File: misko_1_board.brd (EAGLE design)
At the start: 115 x 115 mm, 152 parts, among them IC1 ATMEGA1281-16AU, IC10 ORG1510-MK4, IC11 TPS3808G33DBVT, IC12 LTC4425, IC13 RN4678_BT_MODULE, IC14 ADXL345, IC15 74HCT1G32, IC16 FM25W256-SOIC, IC17 MICROSD_SPI_MODE, IC18 FH12-30S-0.5SH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

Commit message: - crude device driver for the FM25W256 FeRAM SPI device
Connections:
- net SPI_FRAM_SS_PIN renamed SPI_SS_FRAM_PIN
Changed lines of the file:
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@@
 <wire x1="27.5" y1="48.93660625" x2="27.56339375" y2="49" width="0.25" layer="1"/>
 </signal>
-<signal name="SPI_FRAM_SS_PIN" class="2">
+<signal name="SPI_SS_FRAM_PIN" class="2">
 <contactref element="IC16" pad="!CS!"/>
 <contactref element="R19" pad="1"/>

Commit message: - corrected EN pulldown resistor value to 10k
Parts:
- R2: value 150k -> 10k
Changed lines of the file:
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@@
 <grid distance="0.25" unitdist="mm" unit="mm" style="lines" multiple="1" display="yes" altdistance="0.005" altunitdist="mm" altunit="mm"/>
 <layers>
-<layer number="1" name="Top" color="4" fill="1" visible="no" active="yes"/>
+<layer number="1" name="Top" color="4" fill="1" visible="yes" active="yes"/>
 <layer number="2" name="Route2" color="1" fill="3" visible="no" active="no"/>
 <layer number="3" name="Route3" color="4" fill="3" visible="no" active="no"/>
@@
 <layer number="19" name="Unrouted" color="6" fill="1" visible="yes" active="yes"/>
 <layer number="20" name="Dimension" color="15" fill="1" visible="yes" active="yes"/>
-<layer number="21" name="tPlace" color="7" fill="1" visible="no" active="yes"/>
+<layer number="21" name="tPlace" color="7" fill="1" visible="yes" active="yes"/>
 <layer number="22" name="bPlace" color="7" fill="1" visible="yes" active="yes"/>
-<layer number="23" name="tOrigins" color="15" fill="1" visible="no" active="yes"/>
+<layer number="23" name="tOrigins" color="15" fill="1" visible="yes" active="yes"/>
 <layer number="24" name="bOrigins" color="15" fill="1" visible="yes" active="yes"/>
-<layer number="25" name="tNames" color="7" fill="1" visible="no" active="yes"/>
+<layer number="25" name="tNames" color="7" fill="1" visible="yes" active="yes"/>
 <layer number="26" name="bNames" color="7" fill="1" visible="yes" active="yes"/>
 <layer number="27" name="tValues" color="7" fill="1" visible="no" active="yes"/>
@@
 <layer number="37" name="tTest" color="7" fill="1" visible="no" active="yes"/>
 <layer number="38" name="bTest" color="7" fill="1" visible="no" active="yes"/>
-<layer number="39" name="tKeepout" color="4" fill="11" visible="no" active="yes"/>
+<layer number="39" name="tKeepout" color="4" fill="11" visible="yes" active="yes"/>
 <layer number="40" name="bKeepout" color="1" fill="11" visible="yes" active="yes"/>
-<layer number="41" name="tRestrict" color="4" fill="10" visible="no" active="yes"/>
+<layer number="41" name="tRestrict" color="4" fill="10" visible="yes" active="yes"/>
 <layer number="42" name="bRestrict" color="1" fill="10" visible="yes" active="yes"/>
 <layer number="43" name="vRestrict" color="2" fill="10" visible="no" active="yes"/>
@@
 <layer number="45" name="Holes" color="7" fill="1" visible="yes" active="yes"/>
 <layer number="46" name="Milling" color="3" fill="1" visible="yes" active="yes"/>
-<layer number="47" name="Measures" color="7" fill="1" visible="yes" active="yes"/>
+<layer number="47" name="Measures" color="7" fill="1" visible="no" active="yes"/>
 <layer number="48" name="Document" color="7" fill="1" visible="yes" active="yes"/>
 <layer number="49" name="Reference" color="7" fill="1" visible="no" active="yes"/>
 <layer number="50" name="dxf" color="7" fill="1" visible="no" active="no"/>
-<layer number="51" name="tDocu" color="7" fill="1" visible="no" active="yes"/>
+<layer number="51" name="tDocu" color="7" fill="1" visible="yes" active="yes"/>
 <layer number="52" name="bDocu" color="7" fill="1" visible="yes" active="yes"/>
 <layer number="53" name="tGND_GNDA" color="7" fill="9" visible="no" active="no"/>
@@
 <attribute name="VALUE" x="17.865" y="57.04" size="1.27" layer="28" rot="MR180"/>
 </element>
-<element name="R2" library="resistor" library_urn="urn:adsk.eagle:library:348" package="R0805" value="150k" x="76" y="62.49" smashed="yes" rot="MR270">
+<element name="R2" library="resistor" library_urn="urn:adsk.eagle:library:348" package="R0805" value="10k" x="76" y="62.49" smashed="yes" rot="MR270">
 <attribute name="NAME" x="78.14" y="62.49" size="1" layer="26" font="vector" rot="MR90" align="center"/>
 <attribute name="VALUE" x="78.54" y="63.125" size="1.27" layer="28" rot="MR270"/>

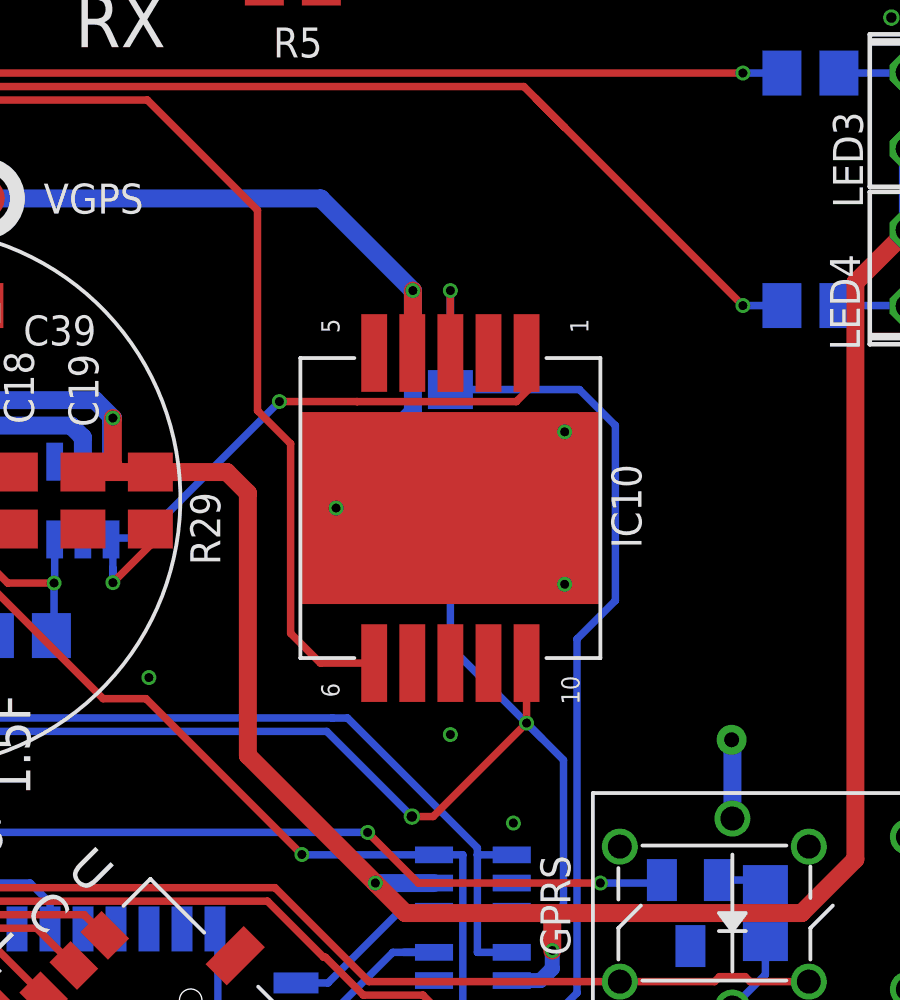
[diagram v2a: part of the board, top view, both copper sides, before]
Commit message: - cleaned up up the GPS module's library
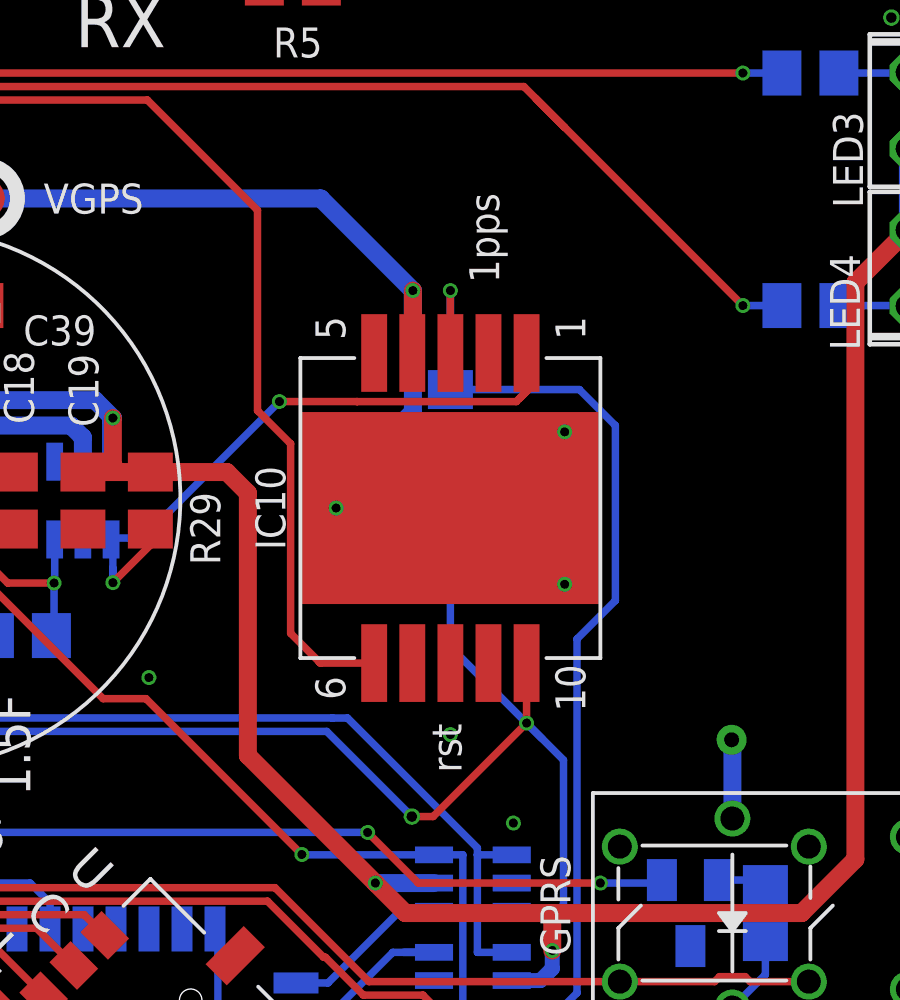
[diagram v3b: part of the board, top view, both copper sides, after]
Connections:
- net GND: now also IC10.GND1; no longer IC10.GND6
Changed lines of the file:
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@@
 <attribute name="VALUE" x="53.492" y="33.488" size="0.0254" layer="27"/>
-</element>
-<element name="IC10" library="ORG1510-MK4 GPS module" package="PACKAGE" value="ORG1510-MK4" x="98.5" y="36.25" smashed="yes" rot="R90">
-<attribute name="NAME" x="104.37" y="36.31" size="1" layer="25" font="vector" rot="R270" align="center"/>
-<attribute name="VALUE" x="107.39" y="32.44" size="1.27" layer="27" rot="R90"/>
 </element>
 <element name="SW1" library="Wurth_Elektronik_Electromechanic_Switch_rev17c" library_urn="urn:adsk.eagle:library:480" package="430152050836" value="RESET" x="29" y="5.5" smashed="yes" rot="R180">
@@
 </element>
 <element name="R23" library="resistor" library_urn="urn:adsk.eagle:library:348" package="R0805" value="10k" x="84.25" y="32" rot="MR0"/>
+<element name="IC10" library="ORG1510-MK4 GPS module" package="PACKAGE" value="ORG1510-MK4" x="98.5" y="36.25" rot="R90"/>
 </elements>
 <signals>
@@
 <contactref element="C35" pad="-"/>
 <contactref element="C38" pad="-"/>
-<contactref element="IC10" pad="GND2"/>
-<contactref element="IC10" pad="GND3"/>
-<contactref element="IC10" pad="GND4"/>
-<contactref element="IC10" pad="GND5"/>
-<contactref element="IC10" pad="GND6"/>
 <contactref element="SW1" pad="1"/>
 <contactref element="SW1" pad="3"/>
@@
 <contactref element="D7" pad="AN"/>
 <contactref element="R23" pad="2"/>
+<contactref element="IC10" pad="GND2"/>
+<contactref element="IC10" pad="GND5"/>
+<contactref element="IC10" pad="GND4"/>
+<contactref element="IC10" pad="GND3"/>
+<contactref element="IC10" pad="GND1"/>
 <wire x1="85.5" y1="67" x2="85.49" y2="67.01" width="0" layer="19" extent="16-16"/>
 <wire x1="32.25" y1="41" x2="31.5" y2="44.5" width="0" layer="19" extent="1-1"/>
@@
 </signal>
 <signal name="GPS_WAKEUP_PIN" class="3">
-<contactref element="IC10" pad="WAKEUP"/>
-<wire x1="95.8782625" y1="31" x2="95.96" y2="31.0817375" width="0.25" layer="1"/>
 <contactref element="IC1" pad="46"/>
 <wire x1="55.12" y1="53.8942" x2="64.28084375" y2="53.8942" width="0.25" layer="1"/>
 <wire x1="92.071" y1="39.4980375" x2="93.175" y2="38.3940375" width="0.25" layer="1"/>
 <wire x1="92.071" y1="46.179" x2="92.071" y2="39.4980375" width="0.25" layer="1"/>
-<wire x1="95.96" y1="31.0817375" x2="94.1682625" y2="31.0817375" width="0.25" layer="1"/>
 <wire x1="93.175" y1="38.3940375" x2="93.175" y2="32.075" width="0.25" layer="1"/>
-<wire x1="93.175" y1="32.075" x2="94.1682625" y2="31.0817375" width="0.25" layer="1"/>
+<wire x1="94.125" y1="31.125" x2="93.175" y2="32.075" width="0.25" layer="1"/>
+<wire x1="94.125" y1="31.125" x2="94.1682625" y2="31.0817375" width="0.25" layer="1"/>
 <wire x1="68.32504375" y1="49.85" x2="88.4" y2="49.85" width="0.25" layer="1"/>
 <wire x1="64.28084375" y1="53.8942" x2="68.32504375" y2="49.85" width="0.25" layer="1"/>
 <wire x1="88.4" y1="49.85" x2="92.071" y2="46.179" width="0.25" layer="1"/>
+<contactref element="IC10" pad="WAKEUP"/>
+<wire x1="95.96" y1="31.0817375" x2="94.1682625" y2="31.0817375" width="0.25" layer="1"/>
+<wire x1="94.1682625" y1="31.0817375" x2="94.125" y2="31.125" width="0.25" layer="1"/>
 </signal>
 <signal name="ANALOG_SW_CTRL_PIN" class="3">
@@
 <contactref element="IC8" pad="3"/>
 <contactref element="C7" pad="2"/>
-<contactref element="IC10" pad="RX"/>
 <wire x1="100.48414375" y1="22.8102" x2="100.5454" y2="22.8102" width="0.25" layer="16"/>
 <via x="101.04" y="29.081734375" extent="1-16" drill="0.3"/>
 <wire x1="100.5454" y1="22.8102" x2="100.978" y2="22.8102" width="0.25" layer="16"/>
 <wire x1="69.2968" y1="33.562275" x2="69.2968" y2="40.812275" width="0.25" layer="16"/>
-<wire x1="101.04" y1="29.081734375" x2="101.04" y2="31.081734375" width="0.25" layer="1"/>
 <wire x1="101.04" y1="22.8722" x2="100.978" y2="22.8102" width="0.25" layer="16"/>
 <wire x1="101.25700625" y1="22.8102" x2="100.5454" y2="22.8102" width="0.25" layer="16"/>
@@
 <via x="97.216840625" y="25.966840625" extent="1-16" drill="0.35"/>
 <wire x1="97.216840625" y1="25.966840625" x2="97.92510625" y2="25.966840625" width="0.25" layer="1"/>
-<wire x1="97.92510625" y1="25.966840625" x2="101.04" y2="29.081734375" width="0.25" layer="1"/>
+<wire x1="101.04" y1="29.081734375" x2="97.92510625" y2="25.966840625" width="0.25" layer="1"/>
 <wire x1="74.0545375" y1="28.8045375" x2="94.37914375" y2="28.8045375" width="0.25" layer="16"/>
 <wire x1="98.5" y1="34.05" x2="98.5" y2="31.621734375" width="0.25" layer="16"/>
@@
 <wire x1="102" y1="22.75" x2="102.271" y2="23.021" width="0.25" layer="16"/>
 <wire x1="102.271" y1="23.021" x2="102.271" y2="27.850734375" width="0.25" layer="16"/>
+<contactref element="IC10" pad="RX"/>
+<wire x1="101.04" y1="31.081734375" x2="101.04" y2="29.081734375" width="0.25" layer="1"/>
 </signal>
 <signal name="SD_CARD_DETECT_PIN" class="2">
@@
 <contactref element="C1" pad="1"/>
 <contactref element="IC9" pad="1"/>
-<contactref element="IC10" pad="TX"/>
 <via x="98.5" y="43.5" extent="1-16" drill="0.3"/>
-<wire x1="98.5" y1="43.5" x2="98.5" y2="41.418265625" width="0.25" layer="1"/>
 <wire x1="102.721" y1="31.88615" x2="104" y2="33.16515" width="0.25" layer="16"/>
 <wire x1="102.721" y1="20.087675" x2="102.721" y2="31.88615" width="0.25" layer="16"/>
-<wire x1="98.5" y1="40.287915625" x2="98.5" y2="43.5" width="0.25" layer="16"/>
 <wire x1="98.5" y1="40.287915625" x2="98.5" y2="40.2" width="0.25" layer="16"/>
 <wire x1="98.7241625" y1="40.287915625" x2="98.5" y2="40.287915625" width="0.25" layer="16"/>
@@
 <wire x1="97.9546" y1="18.7954" x2="101.428725" y2="18.7954" width="0.25" layer="16"/>
 <wire x1="101.428725" y1="18.7954" x2="102.721" y2="20.087675" width="0.25" layer="16"/>
+<contactref element="IC10" pad="TX"/>
+<wire x1="98.5" y1="40.2" x2="98.5" y2="43.5" width="0.25" layer="16"/>
+<wire x1="98.5" y1="43.5" x2="98.5" y2="41.418265625" width="0.25" layer="1"/>
 </signal>
 <signal name="BLUETOOTH_TX" class="2">
@@
 <contactref element="IC12" pad="VOUT1"/>
 <contactref element="IC12" pad="VOUT2"/>
-<contactref element="IC10" pad="VCC"/>
 <contactref element="C39" pad="1"/>
 <via x="97.25" y="43.5" extent="1-16" drill="0.3"/>
-<wire x1="97.25" y1="43.5" x2="97.25" y2="39.44955625" width="0.6" layer="16"/>
 <wire x1="77.9" y1="38.1" x2="78.65" y2="38.1" width="0.4" layer="16"/>
 <wire x1="78.75" y1="38" x2="78.65" y2="38.1" width="0.4" layer="16"/>
@@
 <wire x1="78.75" y1="37.7" x2="82.3" y2="37.7" width="0.6" layer="16"/>
 <wire x1="82.3" y1="37.7" x2="82.5" y2="37.5" width="0.6" layer="16"/>
-<wire x1="97.23" y1="41.418265625" x2="97.25" y2="41.438265625" width="0.6" layer="1"/>
-<wire x1="97.25" y1="41.438265625" x2="97.25" y2="43.5" width="0.6" layer="1"/>
 <wire x1="82.5" y1="37.5" x2="83.95" y2="37.5" width="0.6" layer="1"/>
 <wire x1="83.95" y1="37.5" x2="84" y2="37.45" width="0.6" layer="1"/>
@@
 <wire x1="82.945" y1="43.005" x2="82.95" y2="43" width="0.6" layer="1"/>
 <wire x1="94.18" y1="46.57" x2="80.5" y2="46.57" width="0.6" layer="16"/>
-<wire x1="94.18" y1="46.57" x2="97.25" y2="43.5" width="0.6" layer="16"/>
+<wire x1="97.25" y1="43.5" x2="94.18" y2="46.57" width="0.6" layer="16"/>
 <wire x1="80.5" y1="46.57" x2="73.995" y2="53.075" width="0.25" layer="16"/>
 <wire x1="73.995" y1="53.075" x2="42.27138125" y2="53.075" width="0.25" layer="16"/>
@@
 <wire x1="82.75" y1="39" x2="85.85321875" y2="39" width="0.6" layer="16"/>
 <wire x1="85.85321875" y1="39" x2="86.25" y2="38.60321875" width="0.6" layer="16"/>
+<contactref element="IC10" pad="VCC"/>
+<wire x1="97.25" y1="43.5" x2="97.25" y2="41.438265625" width="0.6" layer="1"/>
+<wire x1="97.25" y1="41.438265625" x2="97.23" y2="41.418265625" width="0.6" layer="1"/>
+<wire x1="97.25" y1="39.44955625" x2="97.25" y2="43.5" width="0.6" layer="16"/>
 </signal>
 <signal name="PFI" class="2">
@@
 <contactref element="IC11" pad="1"/>
 <contactref element="R29" pad="1"/>
-<contactref element="IC10" pad="ON_OFF"/>
 <wire x1="87.1898" y1="35.2046" x2="87.25" y2="35.1444" width="0.25" layer="16"/>
 <wire x1="87.25" y1="35.1444" x2="87.25" y2="33.764" width="0.25" layer="16"/>
@@
 <wire x1="88.5" y1="35.014" x2="87.25" y2="33.764" width="0.25" layer="1"/>
 <via x="92.8" y="39.8" extent="1-16" drill="0.3"/>
-<wire x1="101.1" y1="40.2" x2="101.1" y2="41.358265625" width="0.25" layer="1"/>
-<wire x1="101.1" y1="41.358265625" x2="101.04" y2="41.418265625" width="0.25" layer="1"/>
 <wire x1="92.8" y1="39.8" x2="95.39144375" y2="39.8" width="0.25" layer="1"/>
 <wire x1="95.39144375" y1="39.8" x2="95.39358125" y2="39.7978625" width="0.25" layer="1"/>
-<wire x1="100.6978625" y1="39.7978625" x2="101.1" y2="40.2" width="0.25" layer="1"/>
+<wire x1="100.825" y1="39.925" x2="100.6978625" y2="39.7978625" width="0.25" layer="1"/>
+<wire x1="100.825" y1="39.925" x2="101.1" y2="40.2" width="0.25" layer="1"/>
 <wire x1="95.39358125" y1="39.7978625" x2="100.6978625" y2="39.7978625" width="0.25" layer="1"/>
 <wire x1="87.25" y1="33.764" x2="87.25" y2="34.25" width="0.25" layer="16"/>
@@
 <wire x1="88.25" y1="35.25" x2="92.8" y2="39.8" width="0.25" layer="16"/>
 <wire x1="87.2352" y1="35.25" x2="88.25" y2="35.25" width="0.25" layer="16"/>
+<contactref element="IC10" pad="ON_OFF"/>
+<wire x1="101.04" y1="41.418265625" x2="101.04" y2="40.14" width="0.25" layer="1"/>
+<wire x1="101.04" y1="40.14" x2="100.825" y2="39.925" width="0.25" layer="1"/>
 </signal>
 <signal name="GSM_ANT" class="2">

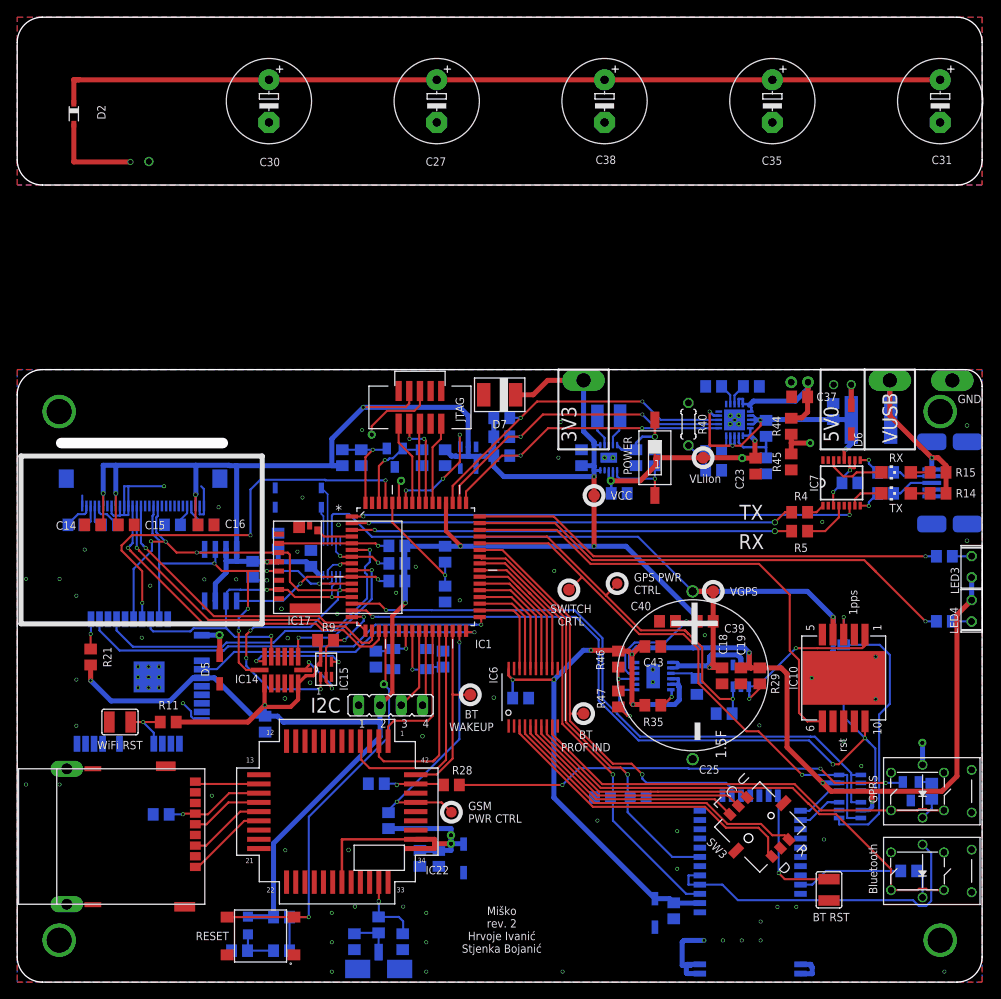
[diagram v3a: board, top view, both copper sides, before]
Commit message: - some more refinements on the GPS lib and on the DRC (now there is a space of 0.5mm between board edge and copper)
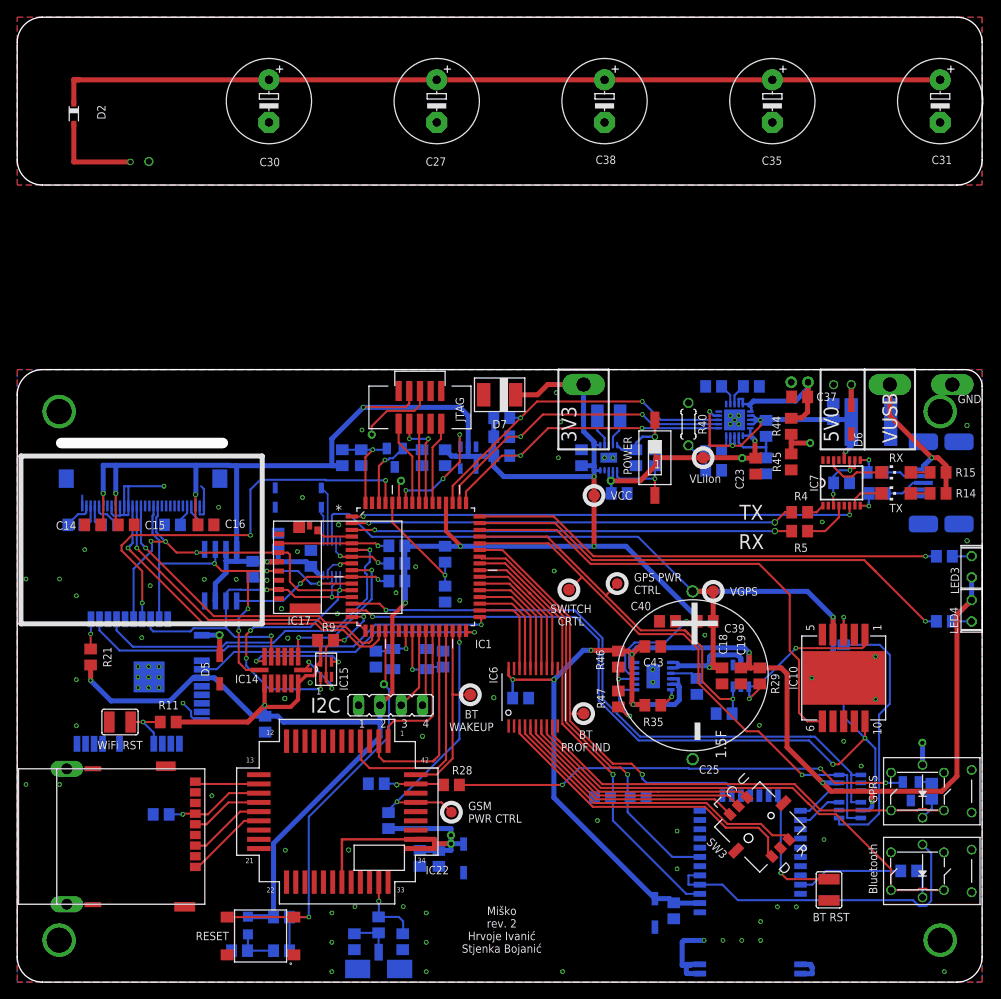
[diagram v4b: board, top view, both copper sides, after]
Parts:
- moved R10 1.25 mm to (102.2, 60.8)
- moved C13 1.00 mm to (98.2, 59.5)
- moved CONN4 1.00 mm to (108.0, 59.5)
- moved R6 1.00 mm to (102.5, 58.2)
- moved TP1 0.50 mm to (111.5, 71.2)
- moved TP2 0.50 mm to (104.0, 71.2)
- moved TP3 0.50 mm to (67.5, 71.2)
- moved L3 0.25 mm to (101.8, 66.8)
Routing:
- net VCC: track 517.4 -> 516.7 mm
- net N$10: track 7.95 -> 8.60 mm
- net JTAG_TDO_PIN: track 11.3 -> 11.8 mm
- net GND: vias 64 -> 65
